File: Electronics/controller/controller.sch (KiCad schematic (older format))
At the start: 23 parts, among them P3 PANEL_2, P4 PANEL_1, P5 DIAL, P6 POWER, P7 SWITCH, P8 LED_DISPLAY, Q1 BUZ11, U1 LM317T, U2 74HC595, U3 Arduino_Pro_Micro

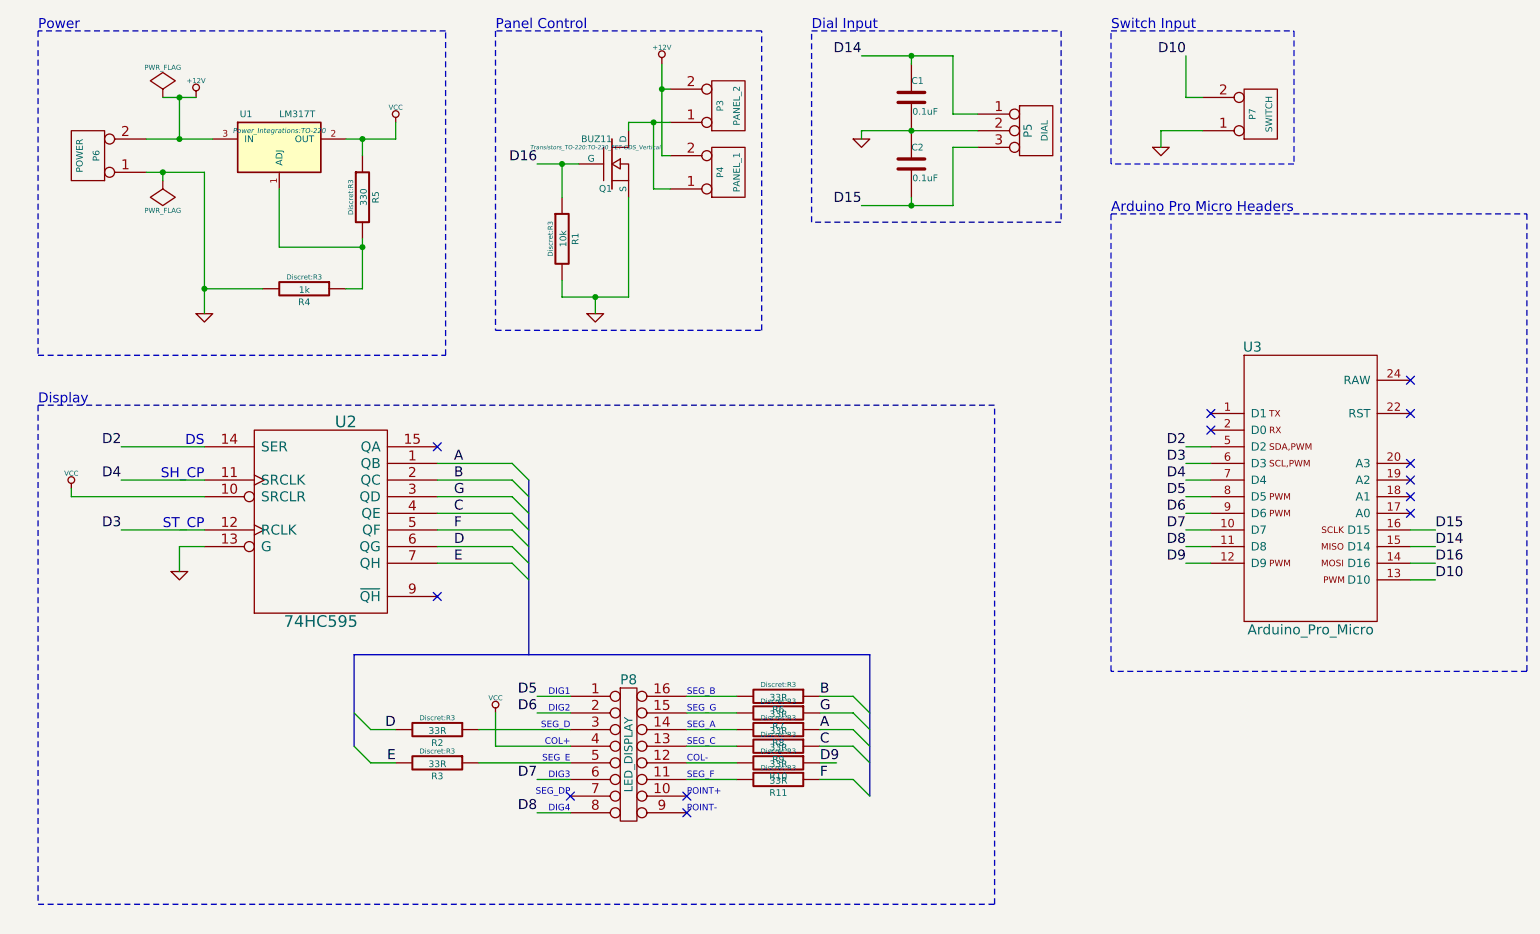
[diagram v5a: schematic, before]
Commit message: Renumbered some sockets. Rerouted pins.
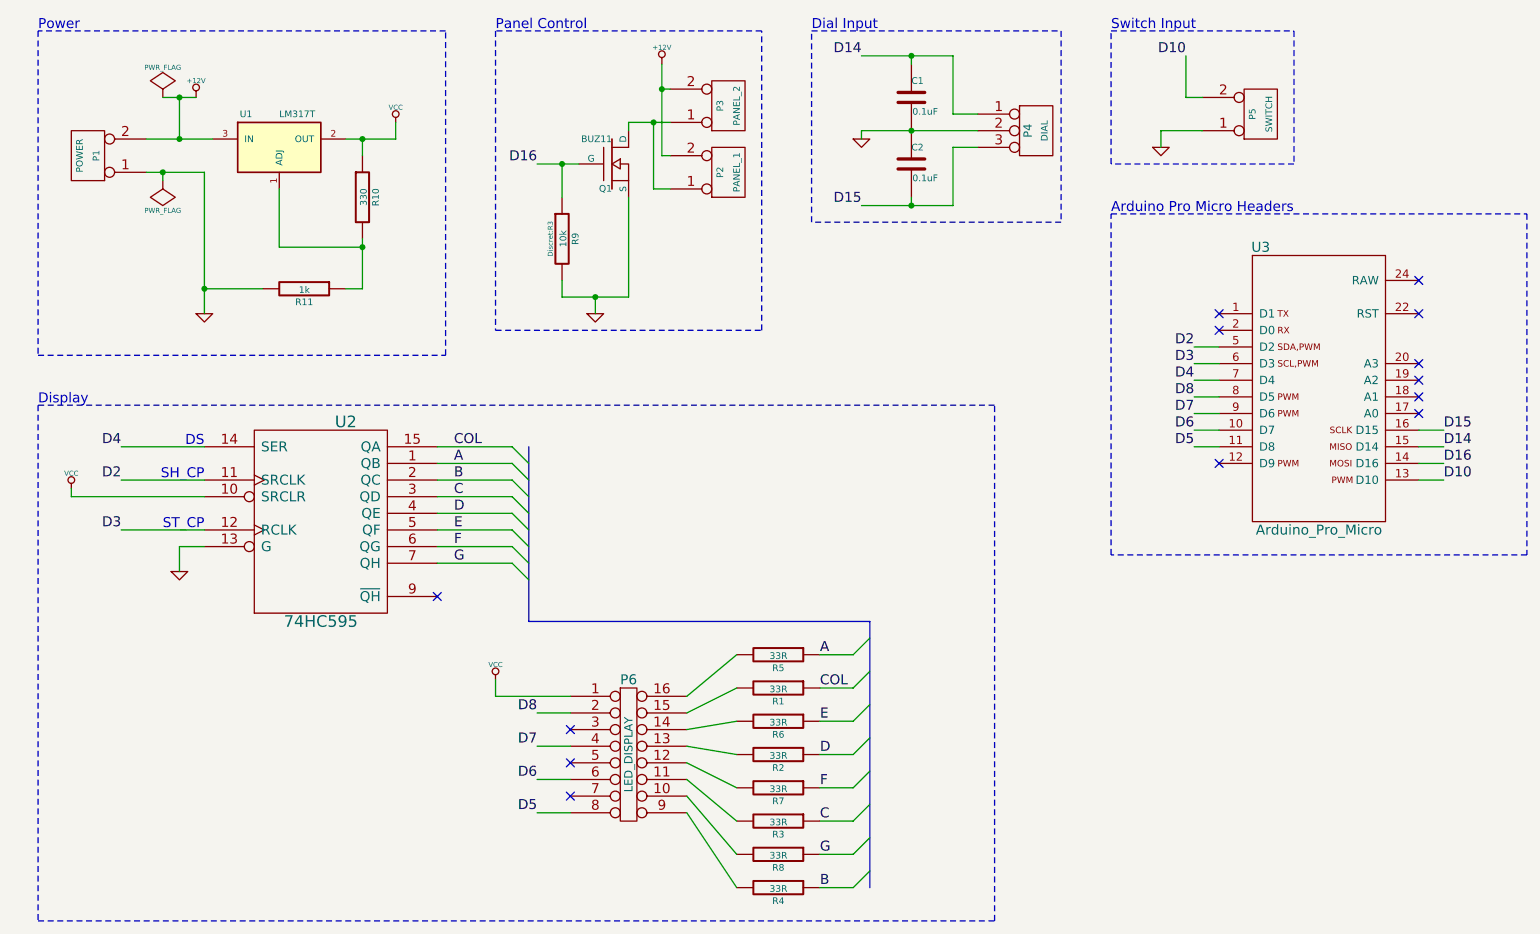
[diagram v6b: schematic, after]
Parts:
- renumbered P6 to P1, P4 to P2, P5 to P4, P7 to P5, P8 to P6, R10 to R1, R5 to R10, R4 to R11, R9 to R3, R11 to R4, R6 to R5, R3 to R6, R8 to R7, R7 to R8, R1 to R9
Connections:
- net A: now also R5.1; no longer R7.1
- net B: now also R4.1; no longer R5.1
- net C: now also U2.3 (QD); no longer U2.4 (QE)
- net D: now also R2.1, U2.4 (QE); no longer R2.2, U2.6 (QG)
- net D2: now also U2.11 (SRCLK); no longer U2.14 (SER)
- net D4: now also U2.14 (SER); no longer U2.11 (SRCLK)
- net D5: now also P6.8, U3.11 (D8); no longer P6.1, U3.8 (D5)
- net D6: now also P6.6, U3.10 (D7); no longer P6.2, U3.9 (D6)
- net D7: now also P6.4, U3.9 (D6); no longer P6.6, U3.10 (D7)
- net D8: now also P6.2, U3.8 (D5); no longer P6.8, U3.11 (D8)
- net E: now also R6.1, U2.5 (QF); no longer R6.2, U2.7 (QH)
- net F: now also R7.1, U2.6 (QG); no longer R4.1, U2.5 (QF)
- net G: now also U2.7 (QH); no longer U2.3 (QD)
- net VCC: now also P6.1; no longer P6.4
- net COL: now reaches U2.15 (QA)
- net COL: now also R1.1
- net at P6.3: no longer R2.1
- net at P6.5: no longer R6.1
- net at P6.10: now also R8.2
- net at P6.11: now also R3.2; no longer R4.2
- net at P6.12: now also R7.2; no longer R1.2
- net at P6.13: now also R2.2; no longer R3.2
- net at P6.14: now also R6.2; no longer R7.2
- net at P6.15: now also R1.2; no longer R8.2
- net at P6.9: now also R4.2
- net D9: no longer names the net of U3.12 (D9)
- net D9: no longer R1.1
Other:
- note removed: "COL+"
- note removed: "COL-"
- note removed: "DIG1"
- note removed: "DIG2"
- note removed: "DIG3"
- note removed: "DIG4"
- note removed: "POINT+"
- note removed: "POINT-"
- note removed: "SEG_A"
- note removed: "SEG_B"
- note removed: "SEG_C"
- note removed: "SEG_D"
- note removed: "SEG_DP"
- note removed: "SEG_E"
- note removed: "SEG_F"
- note removed: "SEG_G"
- moved on the sheet: R1, R2, R3, R4, R5, R6, R7, R8, U3
